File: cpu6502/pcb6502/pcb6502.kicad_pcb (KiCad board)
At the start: 2 copper layers, 11 parts, among them J1 Power Plug, SW1 Reset, U1 6502, U2 EEPROM, U3 RAM, U4 65C22, U5 74HC00, U6 LCD (HD44780), X1 1MHz

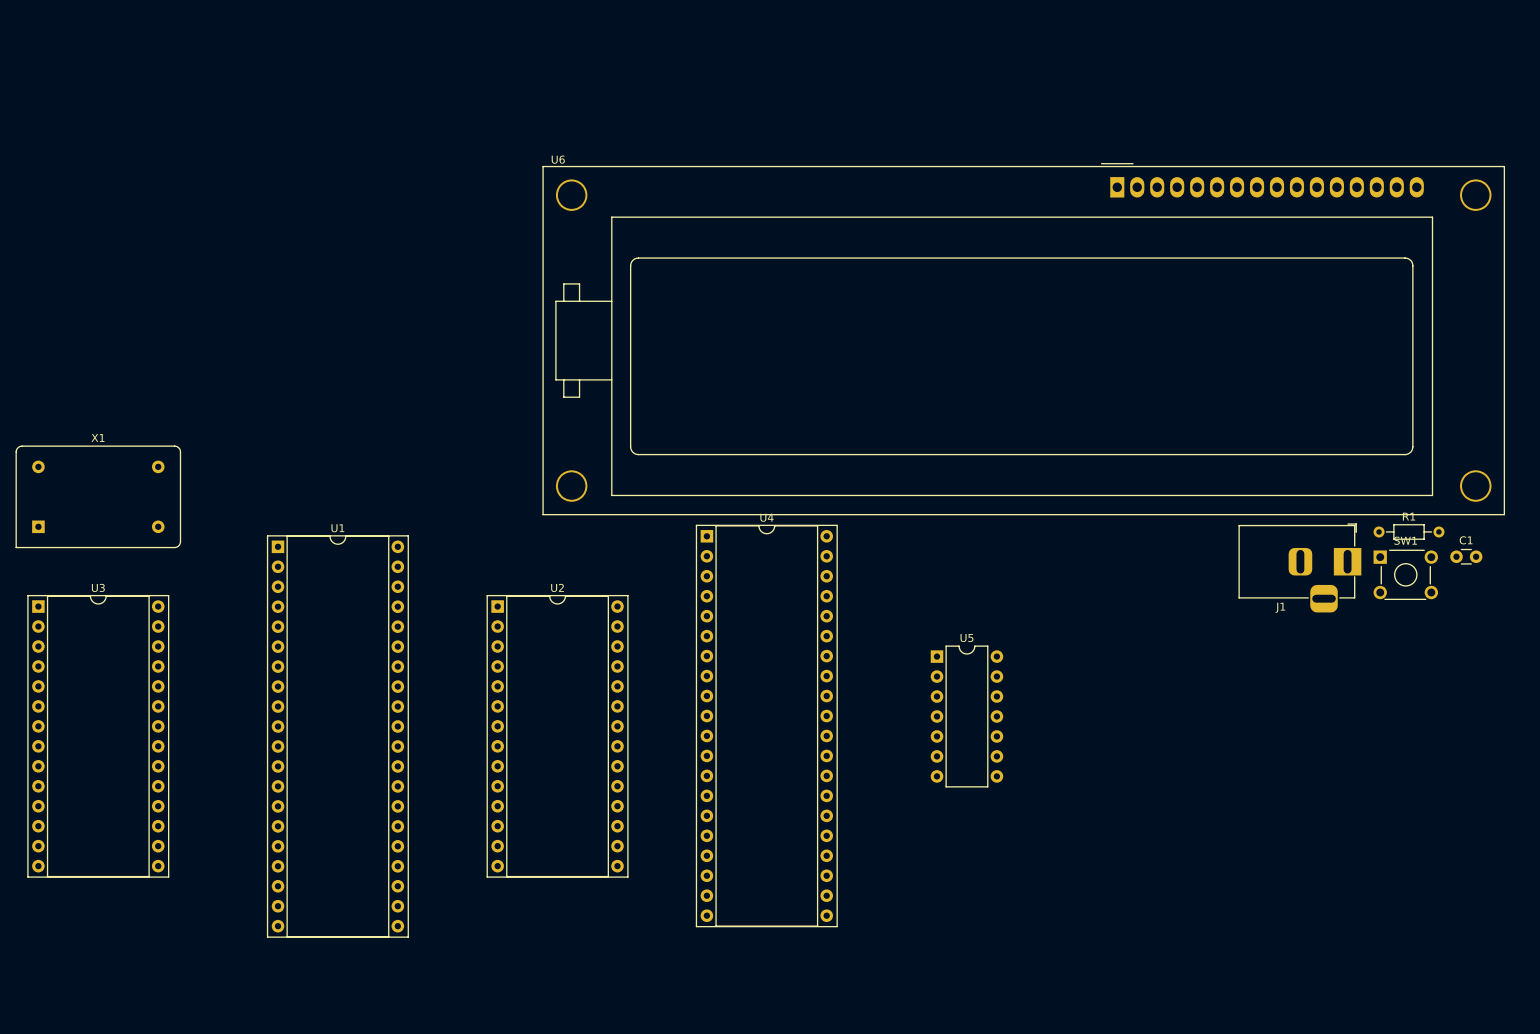
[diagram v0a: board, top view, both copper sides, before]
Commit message: start to add rs232
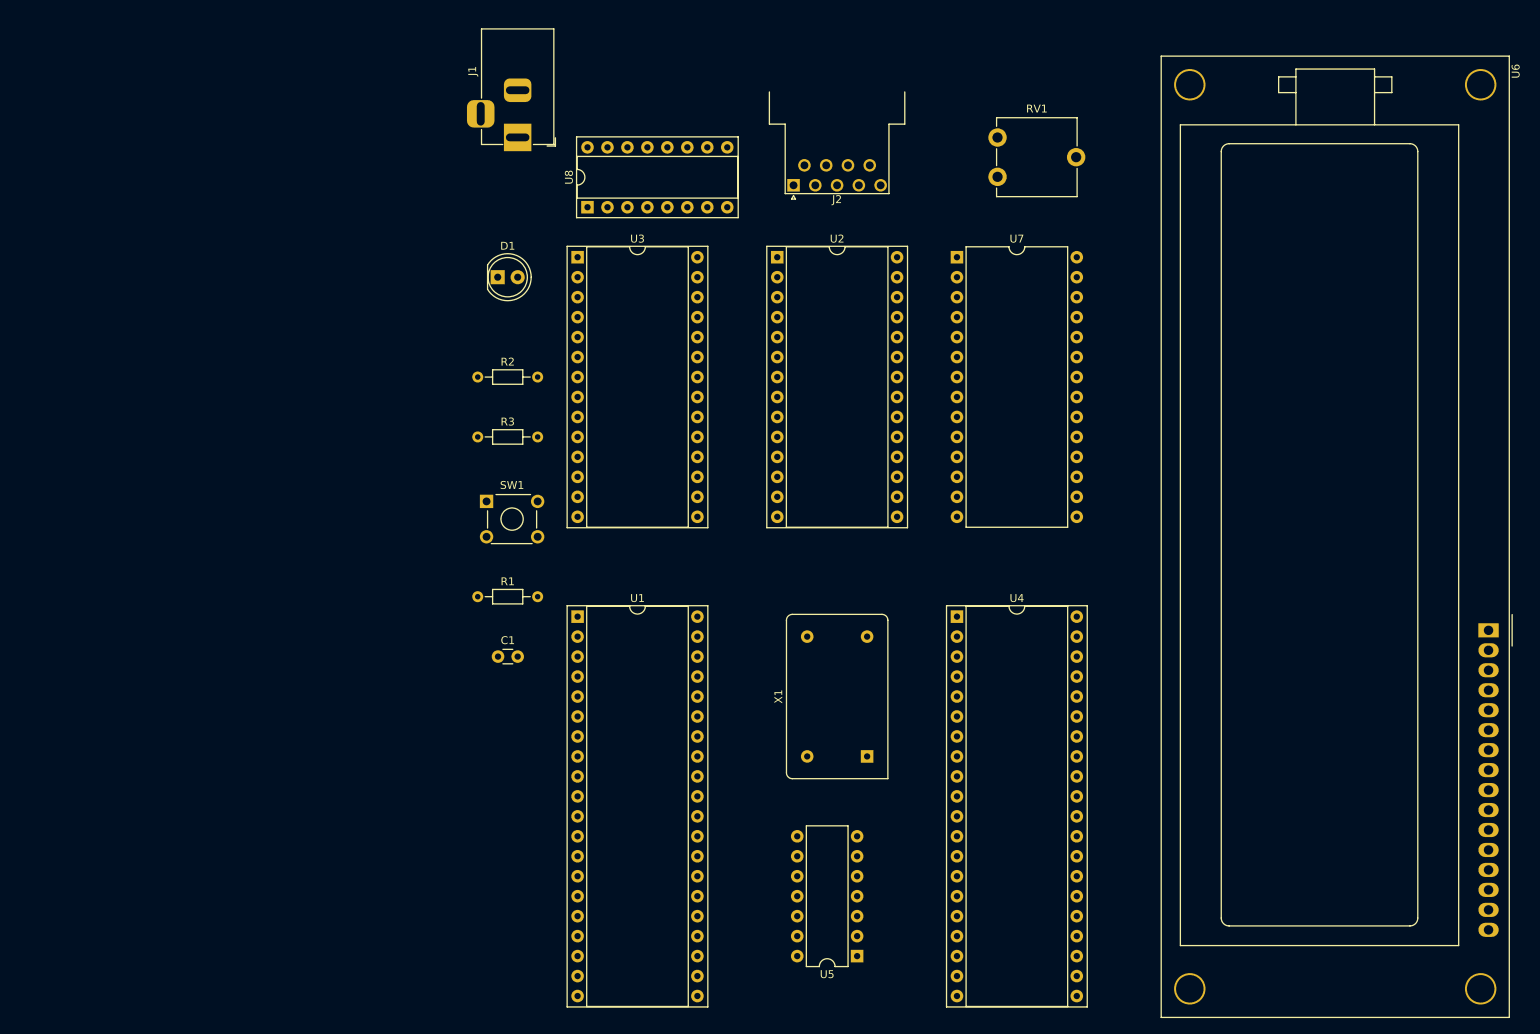
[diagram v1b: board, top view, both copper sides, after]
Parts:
- added D1: Power LED, LED_THT:LED_D5.0mm, F.Cu at (81.3, 55.9)
- added J2: DE9_Receptacle, Connector_Dsub:DSUB-9_Female_Horizontal_P2.77x2.54mm_EdgePinOffset9.40mm, F.Cu at (118.9, 44.2)
- added R2: 220, Resistor_THT:R_Axial_DIN0204_L3.6mm_D1.6mm_P7.62mm_Horizontal, F.Cu at (78.7, 68.6)
- added R3: 1K, Resistor_THT:R_Axial_DIN0204_L3.6mm_D1.6mm_P7.62mm_Horizontal, F.Cu at (78.7, 76.2)
- added RV1: 10K, Potentiometer_THT:Potentiometer_ACP_CA9-V10_Vertical, F.Cu at (144.9, 43.1)
- added U7: W65C51NxP, Package_DIP:DIP-28_W15.24mm, F.Cu at (139.7, 53.3)
- added U8: MAX232, Package_DIP:DIP-16_W7.62mm_Socket, F.Cu at (92.7, 47.0)
- J1: value Power Plug -> 5v Power
- moved C1 122.6 mm to (81.3, 104.1)
- moved J1 118.6 mm to (83.8, 38.1), turned to -90 degrees
- moved R1 114.9 mm to (78.7, 96.5)
- moved SW1 113.9 mm to (79.9, 84.4)
- moved X1 109.4 mm to (128.3, 116.8), turned to 90 degrees
- moved U3 81.7 mm to (91.4, 53.3)
- moved U6 73.5 mm to (207.3, 100.8), turned to -90 degrees
- moved U2 56.9 mm to (116.8, 53.3)
- moved U5 39.4 mm to (127.0, 142.2), turned to 180 degrees
- moved U1 39.1 mm to (91.4, 99.1)
- moved U4 33.4 mm to (139.7, 99.1)
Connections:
- J1 pad 1: unconnected-(J1-Pad1) -> +5V
- J1 pad 2: unconnected-(J1-Pad2) -> GND
- U1 pad 2: unconnected-(U1-RDY-Pad2) -> Net-(U1-RDY)
- U1 pad 21: unconnected-(U1-VSS-Pad21) -> GND
- U1 pad 36: unconnected-(U1-BE-Pad36) -> +5V
- U1 pad 37: unconnected-(U1-ϕ0-Pad37) -> /PHI2
- U1 pad 39: /PHI2 -> unconnected-(U1-ϕ2-Pad39)
- U1 pad 6: unconnected-(U1-~{NMI}-Pad6) -> +5V
- U1 pad 8: unconnected-(U1-VDD-Pad8) -> +5V
- U5 pad 14: unconnected-(U5E-VCC-Pad14) -> +5V
- U5 pad 7: unconnected-(U5E-GND-Pad7) -> GND
- U6 pad 1: unconnected-(U6-LEDK-Pad1) -> /LCD_K
- U6 pad 2: unconnected-(U6-LEDA-Pad2) -> +5V
- U6 pad 3: unconnected-(U6-VSS-Pad3) -> GND
- U6 pad 4: unconnected-(U6-VDD-Pad4) -> +5V
- U6 pad 5: unconnected-(U6-Vo-Pad5) -> /LCD_VO

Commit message: finish rs232, re-layour PCB
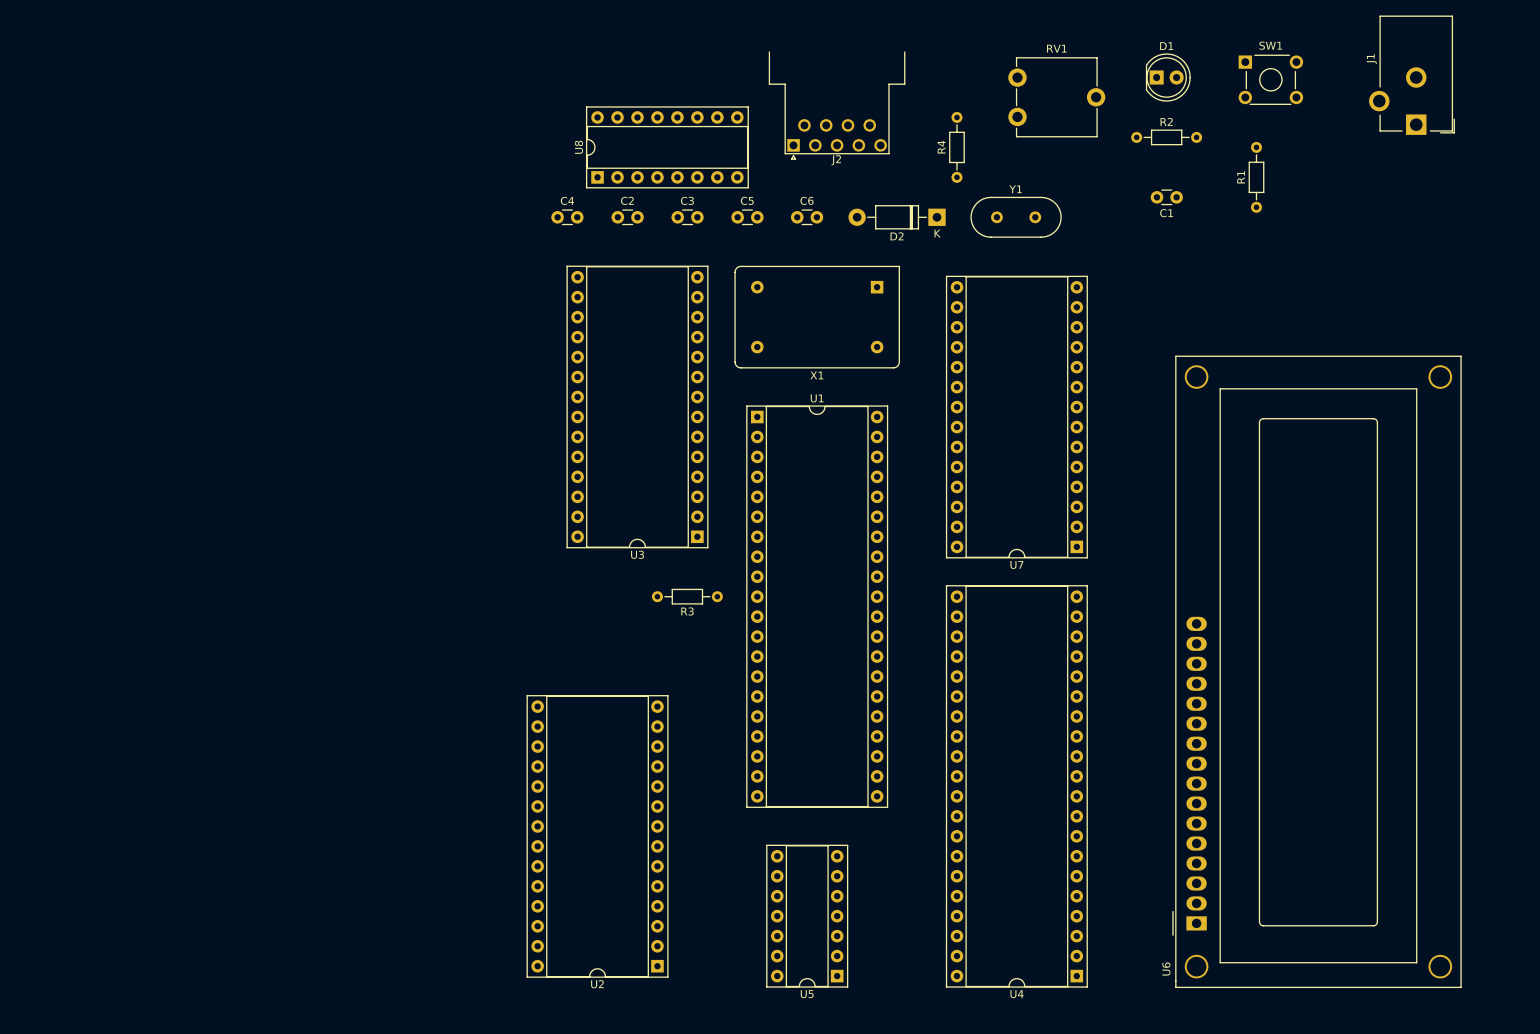
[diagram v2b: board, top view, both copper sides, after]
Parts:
- added C2: 1uf, Capacitor_THT:C_Disc_D3.0mm_W1.6mm_P2.50mm, F.Cu at (96.6, 48.3)
- added C3: 1uf, Capacitor_THT:C_Disc_D3.0mm_W1.6mm_P2.50mm, F.Cu at (104.2, 48.3)
- added C4: 1uf, Capacitor_THT:C_Disc_D3.0mm_W1.6mm_P2.50mm, F.Cu at (88.9, 48.3)
- added C5: 1uf, Capacitor_THT:C_Disc_D3.0mm_W1.6mm_P2.50mm, F.Cu at (111.8, 48.3)
- added C6: 20pf, Capacitor_THT:C_Disc_D3.0mm_W1.6mm_P2.50mm, F.Cu at (119.4, 48.3)
- added D2: SB140, Diode_THT:D_DO-41_SOD81_P10.16mm_Horizontal, F.Cu at (137.2, 48.3)
- added R4: 1M, Resistor_THT:R_Axial_DIN0204_L3.6mm_D1.6mm_P7.62mm_Horizontal, F.Cu at (139.7, 43.2)
- added Y1: Crystal, Crystal:Crystal_HC49-4H_Vertical, F.Cu at (144.8, 48.3)
- J1: footprint Connector_BarrelJack:BarrelJack_Horizontal -> Connector_BarrelJack:BarrelJack_CUI_PJ-102AH_Horizontal
- J2: value DE9_Receptacle -> RS232
- U5: footprint Package_DIP:DIP-14_W7.62mm -> Package_DIP:DIP-14_W7.62mm_Socket
- U6: footprint Display:HY1602E -> Display:WC1602A
- U7: footprint Package_DIP:DIP-28_W15.24mm -> Package_DIP:DIP-28_W15.24mm_Socket
- moved J1 114.3 mm to (198.1, 36.5), turned to 180 degrees
- moved SW1 111.5 mm to (176.4, 28.5)
- moved R1 110.8 mm to (177.8, 47.0), turned to 90 degrees
- moved C1 104.2 mm to (167.6, 45.7), turned to 180 degrees
- moved U2 91.5 mm to (101.6, 143.5), turned to 180 degrees
- moved R2 89.2 mm to (162.6, 38.1)
- moved D1 87.6 mm to (165.1, 30.5)
- moved X1 59.7 mm to (129.5, 57.1), turned to 180 degrees
- moved U6 52.6 mm to (170.2, 138.1), turned to 90 degrees
- moved U4 48.2 mm to (154.9, 144.8), turned to 180 degrees
- moved U7 39.9 mm to (154.9, 90.2), turned to 180 degrees
- moved U3 38.7 mm to (106.7, 88.9), turned to 180 degrees
- moved R3 36.6 mm to (109.2, 96.5), turned to 180 degrees
- moved U1 34.2 mm to (114.3, 73.7)
- moved RV1 8.03 mm to (147.4, 35.5)
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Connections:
- J1 pad 3: (no net) -> GND
- J2 pad 2: unconnected-(J2-Pad2) -> Net-(U8-T1OUT)
- J2 pad 3: unconnected-(J2-Pad3) -> Net-(U8-R1IN)
- J2 pad 5: unconnected-(J2-Pad5) -> GND
- U7 pad 1: unconnected-(U7-VSS-Pad1) -> GND
- U7 pad 10: unconnected-(U7-TxD-Pad10) -> /TxD
- U7 pad 12: unconnected-(U7-RxD-Pad12) -> /RxD
- U7 pad 13: unconnected-(U7-RS0-Pad13) -> /A0
- U7 pad 14: unconnected-(U7-RS1-Pad14) -> /A1
- U7 pad 15: unconnected-(U7-VCC-Pad15) -> +5V
- U7 pad 18: unconnected-(U7-D0-Pad18) -> /D0
- U7 pad 19: unconnected-(U7-D1-Pad19) -> /D1
- U7 pad 2: unconnected-(U7-CS1-Pad2) -> /A12
- U7 pad 20: unconnected-(U7-D2-Pad20) -> /D2
- U7 pad 21: unconnected-(U7-D3-Pad21) -> /D3
- U7 pad 22: unconnected-(U7-D4-Pad22) -> /D4
- U7 pad 23: unconnected-(U7-D5-Pad23) -> /D5
- U7 pad 24: unconnected-(U7-D6-Pad24) -> /D6
- U7 pad 25: unconnected-(U7-D7-Pad25) -> /D7
- U7 pad 26: unconnected-(U7-~{IRQ}-Pad26) -> Net-(D2-K)
- U7 pad 27: unconnected-(U7-ϕ2-Pad27) -> /PHI2
- U7 pad 28: unconnected-(U7-R/~{W}-Pad28) -> /R/W
- U7 pad 3: unconnected-(U7-~{CS2}-Pad3) -> /CS2
- U7 pad 4: unconnected-(U7-~{RES}-Pad4) -> /RST
- U7 pad 6: unconnected-(U7-XTAL1-Pad6) -> /XTLA1
- U7 pad 7: unconnected-(U7-XTAL2-Pad7) -> /XTAL2
- U8 pad 1: unconnected-(U8-C1+-Pad1) -> Net-(U8-C1+)
- U8 pad 11: unconnected-(U8-T1IN-Pad11) -> /TxD
- U8 pad 12: unconnected-(U8-R1OUT-Pad12) -> /RxD
- U8 pad 13: unconnected-(U8-R1IN-Pad13) -> Net-(U8-R1IN)
- U8 pad 14: unconnected-(U8-T1OUT-Pad14) -> Net-(U8-T1OUT)
- U8 pad 15: unconnected-(U8-GND-Pad15) -> GND
- U8 pad 16: unconnected-(U8-VCC-Pad16) -> +5V
- U8 pad 2: unconnected-(U8-VS+-Pad2) -> /232_VS+
- U8 pad 3: unconnected-(U8-C1--Pad3) -> Net-(U8-C1-)
- U8 pad 4: unconnected-(U8-C2+-Pad4) -> Net-(U8-C2+)
- U8 pad 5: unconnected-(U8-C2--Pad5) -> Net-(U8-C2-)
- U8 pad 6: unconnected-(U8-VS--Pad6) -> /232_VS-

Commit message: routed PCB!
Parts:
- removed RV1: 10K, Potentiometer_THT:Potentiometer_ACP_CA9-V10_Vertical
- added C7: 1uF, Capacitor_THT:CP_Radial_D5.0mm_P2.50mm, F.Cu at (111.8, 58.4)
- added C8: 0.1uf, Capacitor_THT:C_Disc_D3.0mm_W1.6mm_P2.50mm, F.Cu at (116.9, 45.7)
- added D3: 1N5819, Diode_THT:D_DO-41_SOD81_P10.16mm_Horizontal, F.Cu at (96.5, 50.8)
- added H1: ~, MountingHole:MountingHole_3.2mm_M3_Pad_Via, F.Cu at (83.8, 132.2)
- added H2: ~, MountingHole:MountingHole_3.2mm_M3_Pad_Via, F.Cu at (83.8, 33.0)
- added H3: ~, MountingHole:MountingHole_3.2mm_M3_Pad_Via, F.Cu at (185.4, 33.0)
- added H4: ~, MountingHole:MountingHole_3.2mm_M3_Pad_Via, F.Cu at (185.4, 132.2)
- added J3: VIA PA, Connector_PinHeader_2.54mm:PinHeader_2x06_P2.54mm_Vertical, F.Cu at (94.0, 129.5)
- added J4: VIA PB, Connector_PinHeader_2.54mm:PinHeader_2x06_P2.54mm_Vertical, F.Cu at (114.3, 129.5)
- added J5: Ext RST, Connector_PinHeader_2.54mm:PinHeader_2x01_P2.54mm_Vertical, F.Cu at (134.6, 129.5)
- added U9: ~, Package_TO_SOT_THT:TO-92, F.Cu at (116.8, 53.3)
- J1: value 5v Power -> Power; footprint Connector_BarrelJack:BarrelJack_CUI_PJ-102AH_Horizontal -> Connector_BarrelJack:BarrelJack_Horizontal
- U2: footprint Package_DIP:DIP-28_W15.24mm_Socket -> Package_DIP:DIP-28_600_ZIF_ARIES_28-526-10
- U6: value LCD (HD44780) -> L7805; footprint Display:WC1602A -> Package_TO_SOT_THT:TO-220F-3_Horizontal_TabUp
- moved U6 123.2 mm to (104.1, 34.1), turned to 0 degrees
- moved J1 104.4 mm to (94.0, 44.1), turned to -90 degrees
- moved U3 74.4 mm to (180.3, 78.7), turned to -90 degrees
- moved U4 74.1 mm to (86.4, 116.8), turned to 90 degrees
- moved U2 69.9 mm to (162.6, 109.2)
- moved U8 58.6 mm to (152.4, 48.3)
- moved SW1 56.2 mm to (130.2, 60.7), turned to 180 degrees
- moved C4 53.6 mm to (142.3, 53.3)
- moved C6 53.6 mm to (172.8, 53.3)
- moved C5 53.6 mm to (165.1, 53.3)
- moved C2 53.5 mm to (149.9, 53.3)
- moved C3 53.5 mm to (157.5, 53.3)
- moved U5 50.0 mm to (170.2, 124.5), turned to -90 degrees
- moved D1 48.9 mm to (116.8, 38.1)
- moved U7 40.7 mm to (180.3, 58.4), turned to -90 degrees
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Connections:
- D1 pad 1: +5V -> Net-(D1-K)
- D1 pad 2: Net-(D1-A) -> +5V
- J1 pad 1: +5V -> Net-(D3-A)
- J1 pad 3: GND -> (no net)
- R2 pad 1: Net-(D1-A) -> Net-(D1-K)
- SW1 pad 1: GND -> Net-(J5-Pin_1)
- U4 pad 18: unconnected-(U4-CB1-Pad18) -> /CB1
- U4 pad 19: unconnected-(U4-CB2-Pad19) -> /CB2
- U4 pad 39: unconnected-(U4-CA2-Pad39) -> /CA2
- U4 pad 40: unconnected-(U4-CA1-Pad40) -> /CA1
- U5 pad 1: unconnected-(U5-Pad1) -> +5V
- U6 pad 1: /LCD_K -> Net-(D3-K)
- U6 pad 2: +5V -> GND
- U6 pad 3: GND -> +5V
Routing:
- net +5V: track 0.00 -> 354.6 mm, vias 0 -> 2
- net /PHI2: track 0.00 -> 219.0 mm, vias 0 -> 1
- net /RST: track 0.00 -> 193.2 mm, vias 0 -> 3
- net /A0: track 0.00 -> 178.6 mm, vias 0 -> 1
- net Net-(J5-Pin_1): track 0.00 -> 168.8 mm
- net /D5: track 0.00 -> 161.3 mm, vias 0 -> 1
- net /D4: track 0.00 -> 160.9 mm, vias 0 -> 5
- net /A1: track 0.00 -> 160.4 mm
- net /R/W: track 0.00 -> 155.5 mm, vias 0 -> 1
- net /D6: track 0.00 -> 155.4 mm
- net /D3: track 0.00 -> 149.2 mm, vias 0 -> 2
- net /D1: track 0.00 -> 136.9 mm, vias 0 -> 1
- net /D2: track 0.00 -> 134.6 mm, vias 0 -> 1
- net /D7: track 0.00 -> 134.2 mm, vias 0 -> 1
- net /A3: track 0.00 -> 129.7 mm
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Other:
- board outline added: 111.8 x 109.2 mm
- board text added: "5V"
- board text added: "CA1"
- board text added: "CA2"
- board text added: "CB1"
- board text added: "CB2"
- board text added: "GND"
- board text added: "PA0"
- board text added: "PA1"
- board text added: "PA2"
- board text added: "PA3"
- board text added: "PA4"
- board text added: "PA5"
- board text added: "PA6"
- board text added: "PA7"
- board text added: "PB0"
- board text added: "PB1"
- board text added: "PB2"
- board text added: "PB3"
- board text added: "PB4"
- board text added: "PB5"
- board text added: "PB6"
- board text added: "PB7"

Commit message: add ground
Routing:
- net GND: track 12.7 -> 632.6 mm, vias 0 -> 6
- net /D0: track 70.5 -> 122.8 mm
- net /A8: track 23.4 -> 74.1 mm
- net +5V: track 354.6 -> 404.3 mm
- net /A11: track 23.4 -> 67.9 mm
- net /A9: track 23.4 -> 66.9 mm
- net /RST: track 193.2 -> 235.4 mm
- net /A15: track 93.7 -> 90.0 mm
- net /IRQ: track 90.8 -> 92.9 mm
- net /PHI2: track 219.0 -> 220.5 mm

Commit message: save for redesign
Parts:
- removed C1: 0.1uf, Capacitor_THT:C_Disc_D3.0mm_W1.6mm_P2.50mm
- removed R1: 1K, Resistor_THT:R_Axial_DIN0204_L3.6mm_D1.6mm_P7.62mm_Horizontal
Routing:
- net /RST: track 235.4 -> 187.3 mm
- net +5V: track 404.3 -> 397.7 mm
- net GND: track 632.6 -> 627.5 mm
- added copper zone on B.Cu, net GND
- added copper zone on F.Cu, net GND
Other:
- board text added: "CG 6502 / RS232 Revision 1.0 2023"
